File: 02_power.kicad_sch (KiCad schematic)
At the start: 48 parts

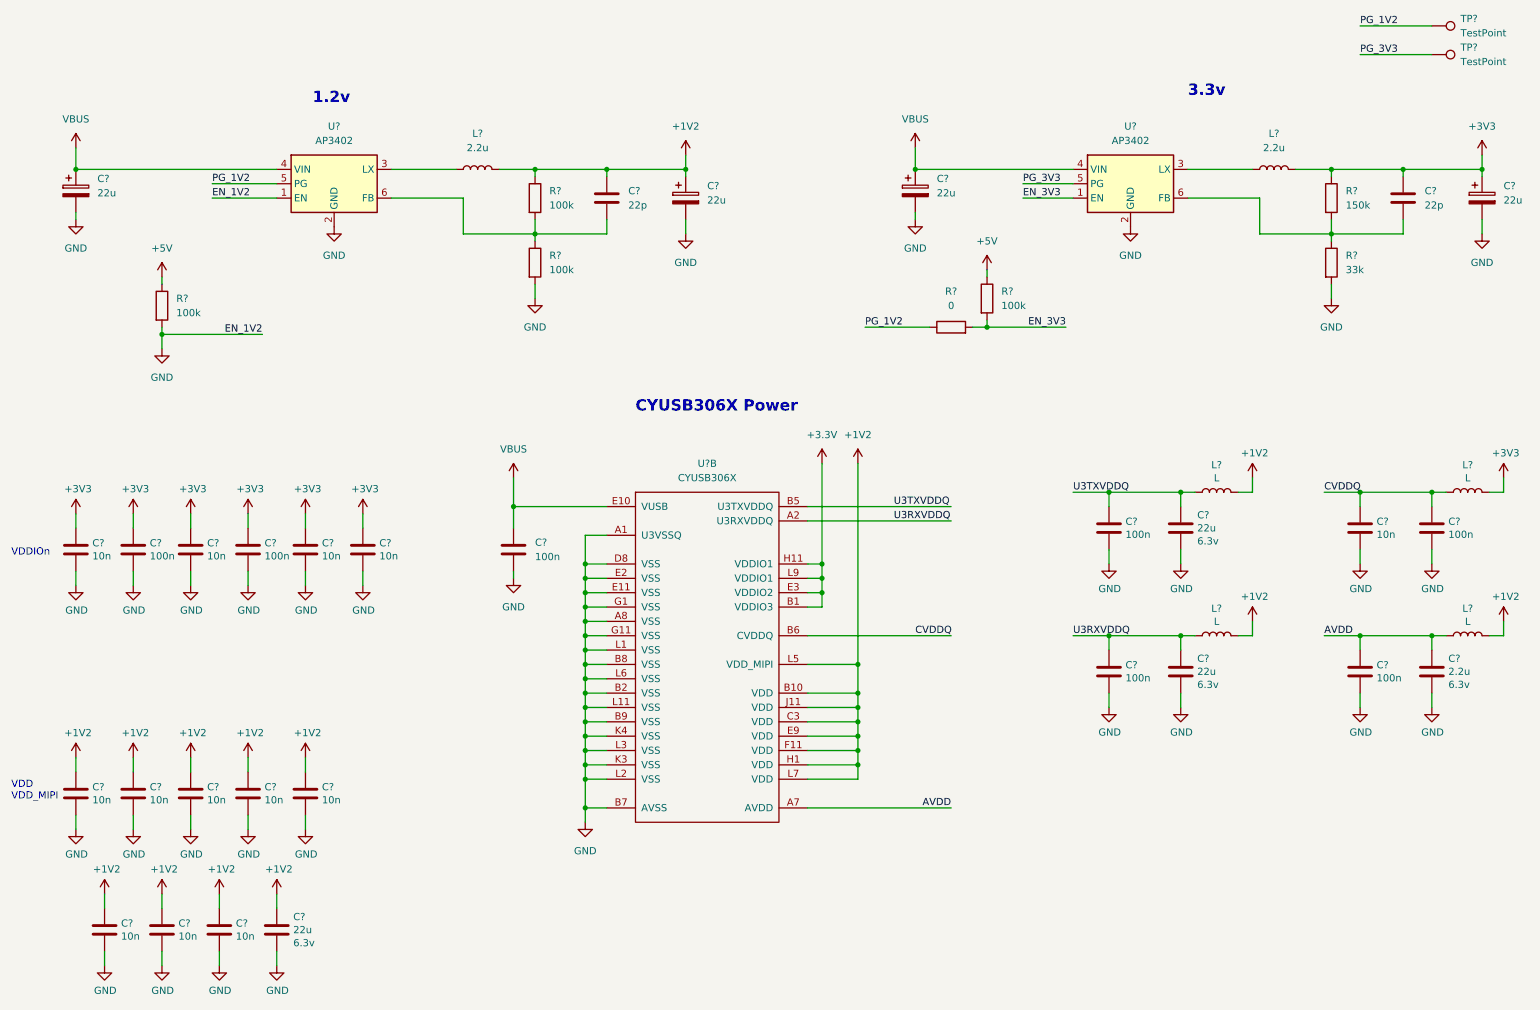
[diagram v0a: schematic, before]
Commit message: cleaned up some DRC errors
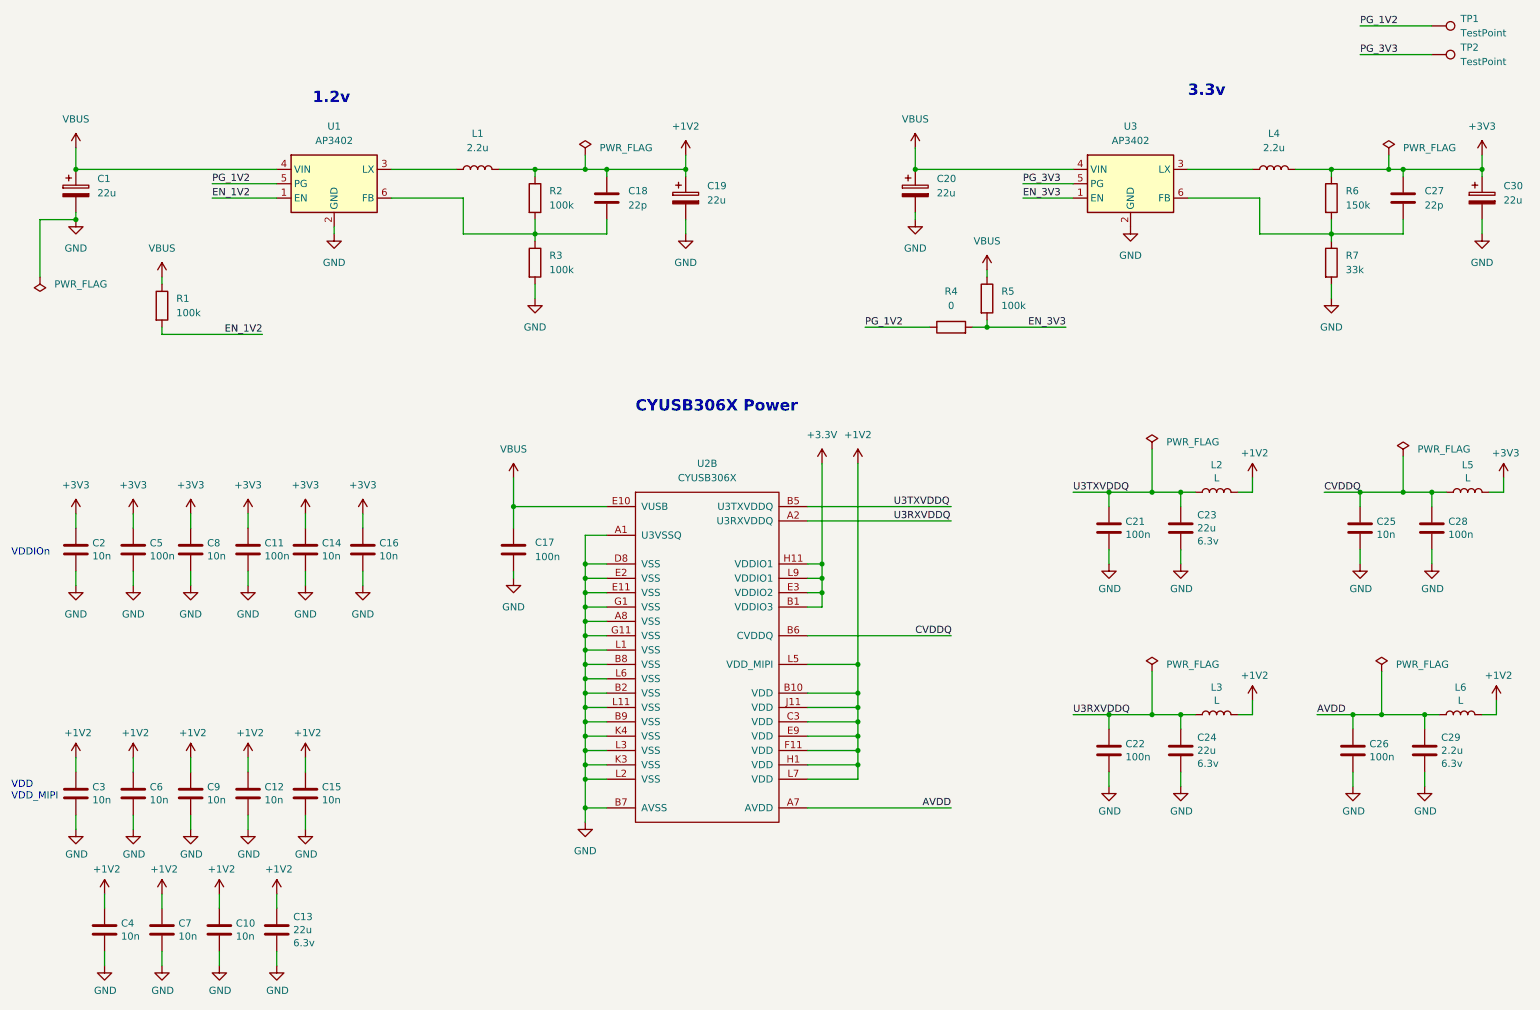
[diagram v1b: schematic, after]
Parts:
- C10, C11, C12, C14, C15, C16, C2, C3, C4, C5, C6, C7, C8, C9: renamed from C?; footprint CSI2USB:C_0402_1005Metric -> Capacitor_SMD:C_0402_1005Metric; symbol CSI2USB:C -> Device:C
- C13: renamed from C?; footprint CSI2USB:C_0805_2012Metric -> Capacitor_SMD:C_0402_1005Metric; symbol CSI2USB:C -> Device:C
- C21, C22, C25, C26, C28: renamed from C?; footprint CSI2USB:C_0402_1005Metric -> Capacitor_SMD:C_0603_1608Metric; symbol CSI2USB:C -> Device:C
- C23, C24, C29: renamed from C?; footprint CSI2USB:C_0805_2012Metric -> Capacitor_SMD:C_0603_1608Metric; symbol CSI2USB:C -> Device:C
- L2, L3, L5, L6: renamed from L?; footprint CSI2USB:L_0603_1608Metric -> Inductor_SMD:L_0603_1608Metric; symbol CSI2USB:L -> Device:L
- gave numbers to parts that had none: 21
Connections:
- net +5V is gone; now on net VBUS: R1.1, R5.1
- net GND: no longer R1.2, U1.1 (EN)
- new net EN_1V2: R1.2, U1.1 (EN)
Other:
- moved on the sheet: C22, C24, C26, C29, L3, L6

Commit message: finished schematics
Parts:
- TP1, TP2: footprint (none) -> TestPoint:TestPoint_THTPad_D1.0mm_Drill0.5mm
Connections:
- net +3.3V is gone; now on net +3V3: U2.B1 (VDDIO3), U2.E3 (VDDIO2), U2.H11 (VDDIO1), U2.L9 (VDDIO1)
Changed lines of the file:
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@@
   (junction (at 219.71 146.05) (diameter 0) (color 0 0 0 0)
   )
+  (junction (at 246.38 49.53) (diameter 0) (color 0 0 0 0)
+  )
+  (junction (at 114.3 129.54) (diameter 0) (color 0 0 0 0)
+  )
   (junction (at 156.21 124.46) (diameter 0) (color 0 0 0 0)
   )
-  (junction (at 246.38 49.53) (diameter 0) (color 0 0 0 0)
-  )
-  (junction (at 114.3 129.54) (diameter 0) (color 0 0 0 0)
-  )
   (junction (at 114.3 121.92) (diameter 0) (color 0 0 0 0)
   )
@@
     (stroke (width 0) (type default) (color 0 0 0 0))
   )
-  (wire (pts (xy 156.21 124.46) (xy 156.21 127))
-    (stroke (width 0) (type default) (color 0 0 0 0))
-  )
   (wire (pts (xy 156.21 121.92) (xy 156.21 124.46))
     (stroke (width 0) (type default) (color 0 0 0 0))
@@
     (stroke (width 0) (type default) (color 0 0 0 0))
   )
+  (wire (pts (xy 153.67 127) (xy 156.21 127))
+    (stroke (width 0) (type default) (color 0 0 0 0))
+  )
   (wire (pts (xy 162.56 147.32) (xy 162.56 149.86))
     (stroke (width 0) (type default) (color 0 0 0 0))
@@
     (stroke (width 0) (type default) (color 0 0 0 0))
   )
-  (wire (pts (xy 156.21 127) (xy 153.67 127))
-    (stroke (width 0) (type default) (color 0 0 0 0))
-  )
   (wire (pts (xy 264.16 106.68) (xy 264.16 109.22))
     (stroke (width 0) (type default) (color 0 0 0 0))
@@
   )
   (wire (pts (xy 114.3 152.4) (xy 114.3 154.94))
+    (stroke (width 0) (type default) (color 0 0 0 0))
+  )
+  (wire (pts (xy 156.21 127) (xy 156.21 124.46))
     (stroke (width 0) (type default) (color 0 0 0 0))
   )
@@
       (effects (font (size 1.27 1.27)) (justify left))
     )
-    (property "Footprint" "" (id 2) (at 264.16 34.29 0)
+    (property "Footprint" "TestPoint:TestPoint_THTPad_D1.0mm_Drill0.5mm" (id 2) (at 264.16 34.29 0)
       (effects (font (size 1.27 1.27)) hide)
     )
@@
     (pin "2")
   )
+  (symbol (lib_id "power:+3V3") (at 156.21 101.6 0) (unit 1)
+    (in_bom yes) (on_board yes)
+    (property "Reference" "#PWR0119" (id 0) (at 156.21 105.41 0)
+      (effects (font (size 1.27 1.27)) hide)
+    )
+    (property "Value" "+3V3" (id 1) (at 156.591 97.2058 0))
+    (property "Footprint" "" (id 2) (at 156.21 101.6 0)
+      (effects (font (size 1.27 1.27)) hide)
+    )
+    (property "Datasheet" "" (id 3) (at 156.21 101.6 0)
+      (effects (font (size 1.27 1.27)) hide)
+    )
+    (pin "1")
+  )
   (symbol (lib_id "power:GND") (at 251.46 119.38 0) (unit 1)
     (in_bom yes) (on_board yes)
@@
       (effects (font (size 1.27 1.27)) (justify left))
     )
-    (property "Footprint" "" (id 2) (at 264.16 29.21 0)
+    (property "Footprint" "TestPoint:TestPoint_THTPad_D1.0mm_Drill0.5mm" (id 2) (at 264.16 29.21 0)
       (effects (font (size 1.27 1.27)) hide)
     )
@@
       (effects (font (size 1.27 1.27)) hide)
     )
-    (pin "1")
-  )
-  (symbol (lib_id "power:+3.3V") (at 156.21 101.6 0) (unit 1)
-    (in_bom yes) (on_board yes) (fields_autoplaced)
-    (property "Reference" "#PWR042" (id 0) (at 156.21 105.41 0)
-      (effects (font (size 1.27 1.27)) hide)
-    )
-    (property "Value" "+3.3V" (id 1) (at 156.21 96.52 0))
-    (property "Footprint" "" (id 2) (at 156.21 101.6 0)
-      (effects (font (size 1.27 1.27)) hide)
-    )
-    (property "Datasheet" "" (id 3) (at 156.21 101.6 0)
-      (effects (font (size 1.27 1.27)) hide)
-    )
